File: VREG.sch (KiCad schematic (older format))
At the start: 100 parts

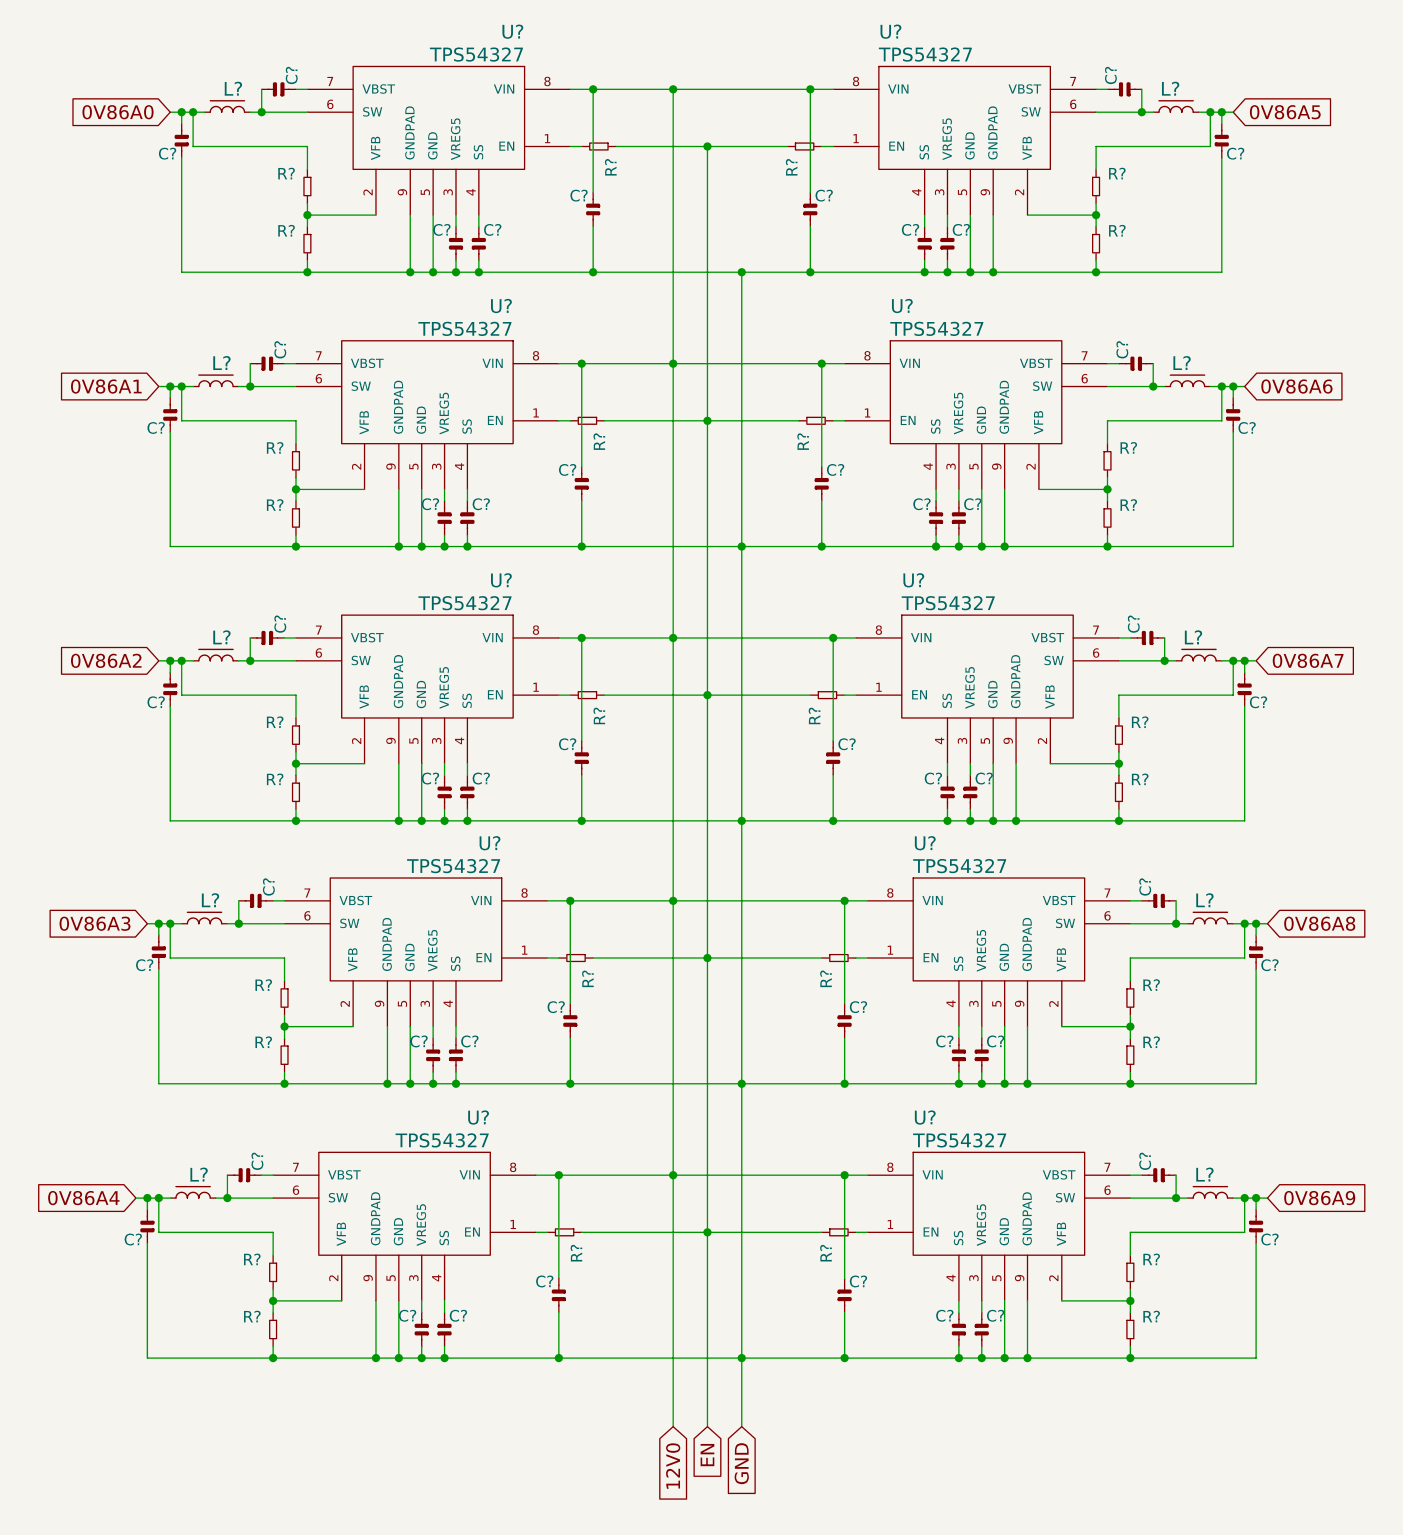
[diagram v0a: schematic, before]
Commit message: Fill in component values in schematic
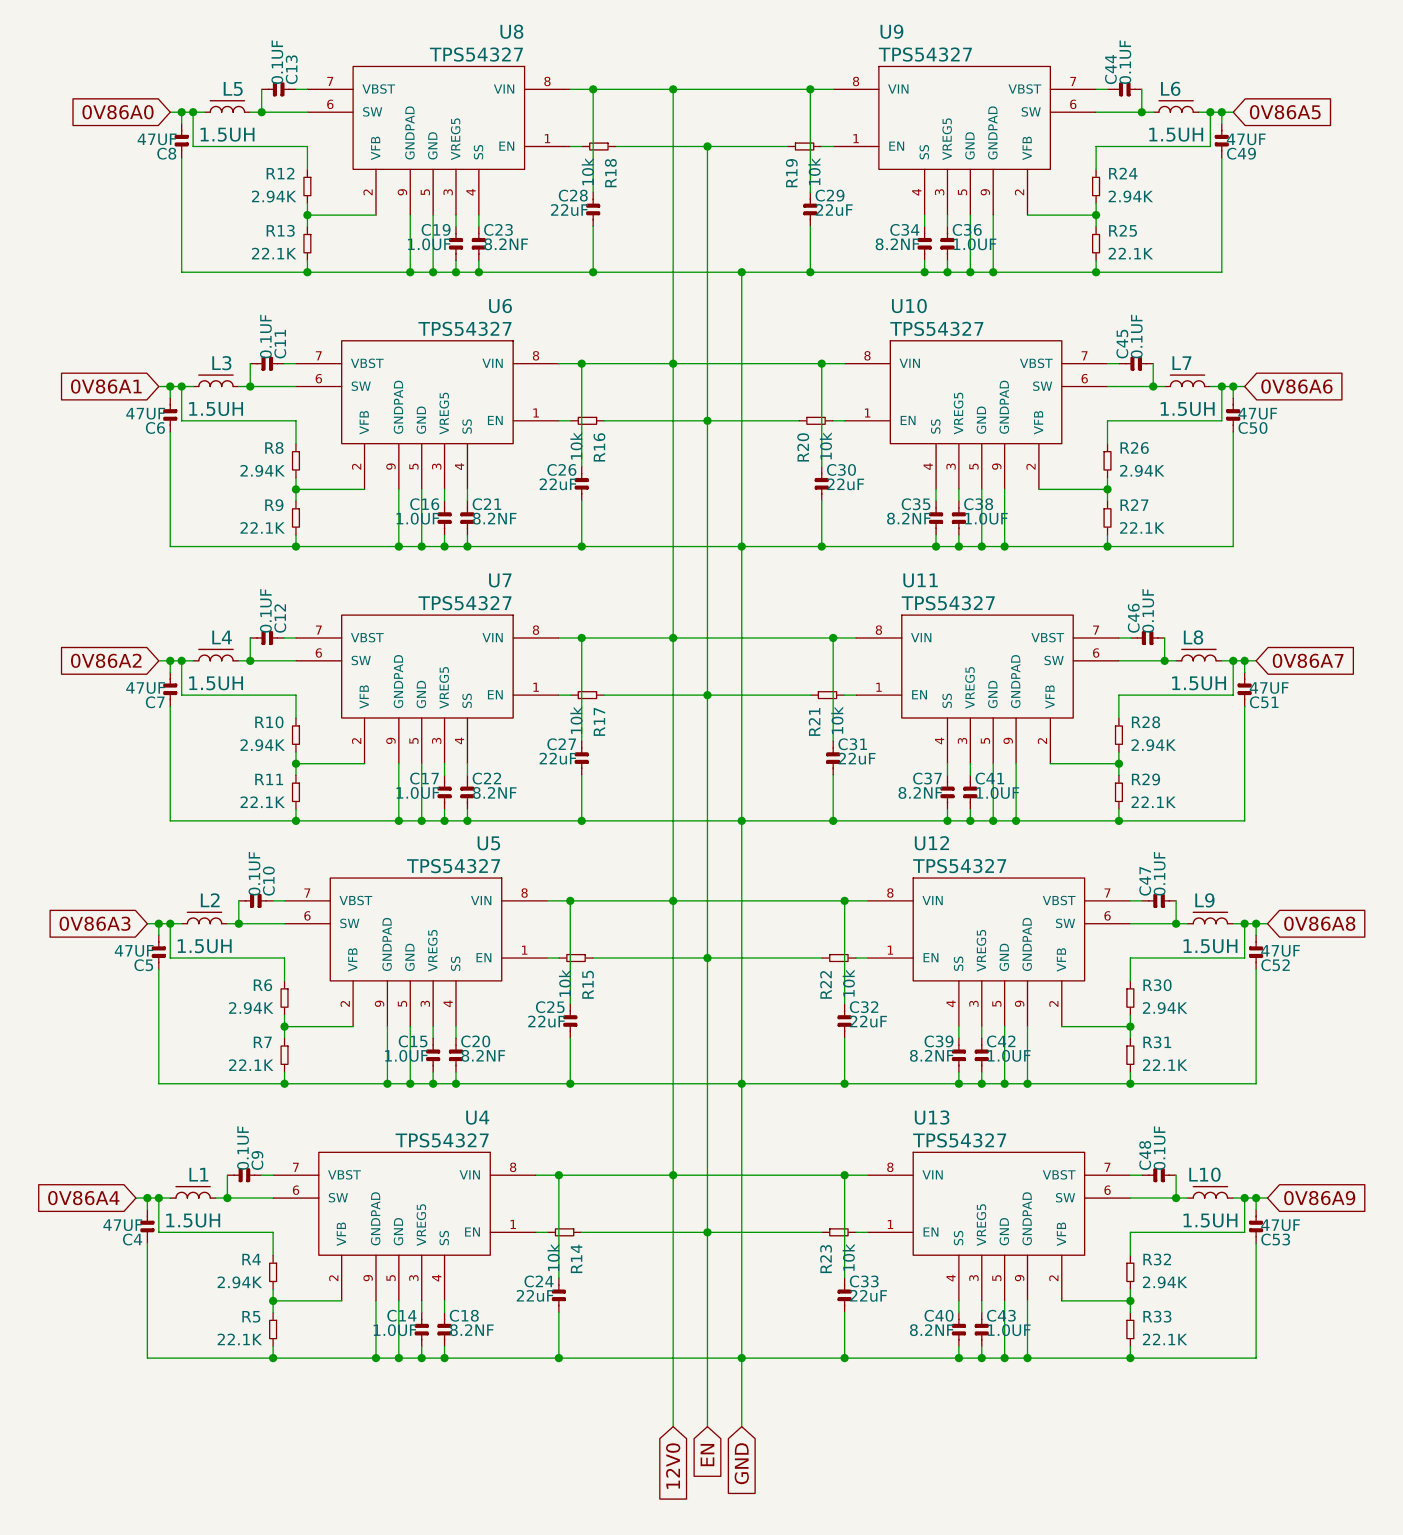
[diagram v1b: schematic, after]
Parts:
- C10, C11, C12, C13, C44, C45, C46, C47, C48, C9: renamed from C?; value CAPACITOR-NONPOLAR -> 0.1UF
- C14, C15, C16, C17, C19, C36, C38, C41, C42, C43: renamed from C?; value CAPACITOR-NONPOLAR -> 1.0UF
- C18, C20, C21, C22, C23, C34, C35, C37, C39, C40: renamed from C?; value CAPACITOR-NONPOLAR -> 8.2NF
- C24, C25, C26, C27, C28, C29, C30, C31, C32, C33: renamed from C?; value CAPACITOR-NONPOLAR -> 22uF
- C4, C49, C5, C50, C51, C52, C53, C6, C7, C8: renamed from C?; value CAPACITOR-NONPOLAR -> 47UF
- L1, L10, L2, L3, L4, L5, L6, L7, L8, L9: renamed from L?; value INDUCTOR-IRONCORE -> 1.5UH
- R10, R12, R24, R26, R28, R30, R32, R4, R6, R8: renamed from R?; value RESISTOR -> 2.94K
- R11, R13, R25, R27, R29, R31, R33, R5, R7, R9: renamed from R?; value RESISTOR -> 22.1K
- R14, R15, R16, R17, R18, R19, R20, R21, R22, R23: renamed from R?; value RESISTOR -> 10k
- gave numbers to parts that had none: 10

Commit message: Added ASIC row 0 and added links for power domains and comm lines
Renumbered components.

Added LED on MCP2210 GP3 pin to show SPI traffic activity (this feature
will require either programming of the NFx to modify NVRAM boot
settings [most likely], or added driver code in mcp init block [less
likely])
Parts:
- renumbered R9 to R10, R10 to R11, R11 to R12, R12 to R13, R13 to R14, R14 to R15, R15 to R16, R16 to R17, R17 to R18, R18 to R19, R19 to R20, R20 to R21, R21 to R22, R22 to R23, R23 to R24, R24 to R25, R25 to R26, R26 to R27, R27 to R28, R28 to R29, R29 to R30, R30 to R31, R31 to R32, R32 to R33, R33 to R34, R4 to R5, R5 to R6, R6 to R7, R7 to R8, R8 to R9
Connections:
- net EN renamed V_EN
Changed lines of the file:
@@
-EESchema Schematic File Version 2  date Sunday, February 23, 2014 'AMt' 01:58:09 AM
+EESchema Schematic File Version 2  date Monday, February 24, 2014 'AMt' 12:37:09 AM
 LIBS:power
 LIBS:74xgxx
@@
 Sheet 2 3
 Title "NanoFury NFx"
-Date "23 feb 2014"
+Date "24 feb 2014"
 Rev "43f0eac2"
 Comp ""
@@
 $EndComp
 $Comp
-L RESISTOR R18
+L RESISTOR R19
 U 1 1 53071CD3
 P 5250 1050
-F 0 "R18" H 5300 1000 50  0000 L BNN
+F 0 "R19" H 5300 1000 50  0000 L BNN
 F 1 "10k" H 5300 900 50  0000 L BNN
 F 2 "" H 5350 1150 50  0001 C CNN
@@
 $EndComp
 $Comp
-L RESISTOR R13
+L RESISTOR R14
 U 1 1 53071E4C
 P 3900 1400
-F 0 "R13" H 3950 1350 50  0000 L BNN
+F 0 "R14" H 3950 1350 50  0000 L BNN
 F 1 "22.1K" H 3950 1250 50  0000 L BNN
 F 2 "" H 4000 1500 50  0001 C CNN
@@
 $EndComp
 $Comp
-L RESISTOR R12
+L RESISTOR R13
 U 1 1 53071E5B
 P 3900 1150
-F 0 "R12" H 3950 1100 50  0000 L BNN
+F 0 "R13" H 3950 1100 50  0000 L BNN
 F 1 "2.94K" H 3950 1000 50  0000 L BNN
 F 2 "" H 4000 1250 50  0001 C CNN
@@
 $EndComp
 $Comp
-L RESISTOR R16
+L RESISTOR R17
 U 1 1 53071F77
 P 5200 2250
-F 0 "R16" H 5250 2200 50  0000 L BNN
+F 0 "R17" H 5250 2200 50  0000 L BNN
 F 1 "10k" H 5250 2100 50  0000 L BNN
 F 2 "" H 5300 2350 50  0001 C CNN
@@
 $EndComp
 $Comp
-L RESISTOR R9
+L RESISTOR R10
 U 1 1 53071F83
 P 3850 2600
-F 0 "R9" H 3900 2550 50  0000 L BNN
+F 0 "R10" H 3900 2550 50  0000 L BNN
 F 1 "22.1K" H 3900 2450 50  0000 L BNN
 F 2 "" H 3950 2700 50  0001 C CNN
@@
 $EndComp
 $Comp
-L RESISTOR R8
+L RESISTOR R9
 U 1 1 53071F89
 P 3850 2350
-F 0 "R8" H 3900 2300 50  0000 L BNN
+F 0 "R9" H 3900 2300 50  0000 L BNN
 F 1 "2.94K" H 3900 2200 50  0000 L BNN
 F 2 "" H 3950 2450 50  0001 C CNN
@@
 $EndComp
 $Comp
-L RESISTOR R17
+L RESISTOR R18
 U 1 1 53071FDA
 P 5200 3450
-F 0 "R17" H 5250 3400 50  0000 L BNN
+F 0 "R18" H 5250 3400 50  0000 L BNN
 F 1 "10k" H 5250 3300 50  0000 L BNN
 F 2 "" H 5300 3550 50  0001 C CNN
@@
 $EndComp
 $Comp
-L RESISTOR R11
+L RESISTOR R12
 U 1 1 53071FE6
 P 3850 3800
-F 0 "R11" H 3900 3750 50  0000 L BNN
+F 0 "R12" H 3900 3750 50  0000 L BNN
 F 1 "22.1K" H 3900 3650 50  0000 L BNN
 F 2 "" H 3950 3900 50  0001 C CNN
@@
 $EndComp
 $Comp
-L RESISTOR R10
+L RESISTOR R11
 U 1 1 53071FEC
 P 3850 3550
-F 0 "R10" H 3900 3500 50  0000 L BNN
+F 0 "R11" H 3900 3500 50  0000 L BNN
 F 1 "2.94K" H 3900 3400 50  0000 L BNN
 F 2 "" H 3950 3650 50  0001 C CNN
@@
 $EndComp
 $Comp
-L RESISTOR R15
+L RESISTOR R16
 U 1 1 5307203D
 P 5150 4600
-F 0 "R15" H 5200 4550 50  0000 L BNN
+F 0 "R16" H 5200 4550 50  0000 L BNN
 F 1 "10k" H 5200 4450 50  0000 L BNN
 F 2 "" H 5250 4700 50  0001 C CNN
@@
 $EndComp
 $Comp
-L RESISTOR R7
+L RESISTOR R8
 U 1 1 53072049
 P 3800 4950
-F 0 "R7" H 3850 4900 50  0000 L BNN
+F 0 "R8" H 3850 4900 50  0000 L BNN
 F 1 "22.1K" H 3850 4800 50  0000 L BNN
 F 2 "" H 3900 5050 50  0001 C CNN
@@
 $EndComp
 $Comp
-L RESISTOR R6
+L RESISTOR R7
 U 1 1 5307204F
 P 3800 4700
-F 0 "R6" H 3850 4650 50  0000 L BNN
+F 0 "R7" H 3850 4650 50  0000 L BNN
 F 1 "2.94K" H 3850 4550 50  0000 L BNN
 F 2 "" H 3900 4800 50  0001 C CNN
@@
 $EndComp
 $Comp
-L RESISTOR R19
+L RESISTOR R20
 U 1 1 530720A0
 P 6000 1050
-F 0 "R19" H 6050 1000 50  0000 L BNN
+F 0 "R20" H 6050 1000 50  0000 L BNN
 F 1 "10k" H 6050 900 50  0000 L BNN
 F 2 "" H 6100 1150 50  0001 C CNN
@@
 $EndComp
 $Comp
-L RESISTOR R25
+L RESISTOR R26
 U 1 1 530720AC
 P 7350 1400
-F 0 "R25" H 7400 1350 50  0000 L BNN
+F 0 "R26" H 7400 1350 50  0000 L BNN
 F 1 "22.1K" H 7400 1250 50  0000 L BNN
 F 2 "" H 7450 1500 50  0001 C CNN
@@
 $EndComp
 $Comp
-L RESISTOR R24
+L RESISTOR R25
 U 1 1 530720B2
 P 7350 1150
-F 0 "R24" H 7400 1100 50  0000 L BNN
+F 0 "R25" H 7400 1100 50  0000 L BNN
 F 1 "2.94K" H 7400 1000 50  0000 L BNN
 F 2 "" H 7450 1250 50  0001 C CNN
@@
 $EndComp
 $Comp
-L RESISTOR R20
+L RESISTOR R21
 U 1 1 53072103
 P 6050 2250
-F 0 "R20" H 6100 2200 50  0000 L BNN
+F 0 "R21" H 6100 2200 50  0000 L BNN
 F 1 "10k" H 6100 2100 50  0000 L BNN
 F 2 "" H 6150 2350 50  0001 C CNN
@@
 $EndComp
 $Comp
-L RESISTOR R27
+L RESISTOR R28
 U 1 1 5307210F
 P 7400 2600
-F 0 "R27" H 7450 2550 50  0000 L BNN
+F 0 "R28" H 7450 2550 50  0000 L BNN
 F 1 "22.1K" H 7450 2450 50  0000 L BNN
 F 2 "" H 7500 2700 50  0001 C CNN
@@
 $EndComp
 $Comp
-L RESISTOR R26
+L RESISTOR R27
 U 1 1 53072115
 P 7400 2350
-F 0 "R26" H 7450 2300 50  0000 L BNN
+F 0 "R27" H 7450 2300 50  0000 L BNN
 F 1 "2.94K" H 7450 2200 50  0000 L BNN
 F 2 "" H 7500 2450 50  0001 C CNN
@@
 $EndComp
 $Comp
-L RESISTOR R21
+L RESISTOR R22
 U 1 1 53072166
 P 6100 3450
-F 0 "R21" H 6150 3400 50  0000 L BNN
+F 0 "R22" H 6150 3400 50  0000 L BNN
 F 1 "10k" H 6150 3300 50  0000 L BNN
 F 2 "" H 6200 3550 50  0001 C CNN
@@
 $EndComp
 $Comp
-L RESISTOR R29
+L RESISTOR R30
 U 1 1 53072172
 P 7450 3800
-F 0 "R29" H 7500 3750 50  0000 L BNN
+F 0 "R30" H 7500 3750 50  0000 L BNN
 F 1 "22.1K" H 7500 3650 50  0000 L BNN
 F 2 "" H 7550 3900 50  0001 C CNN
@@
 $EndComp
 $Comp
-L RESISTOR R28
+L RESISTOR R29
 U 1 1 53072178
 P 7450 3550
-F 0 "R28" H 7500 3500 50  0000 L BNN
+F 0 "R29" H 7500 3500 50  0000 L BNN
 F 1 "2.94K" H 7500 3400 50  0000 L BNN
 F 2 "" H 7550 3650 50  0001 C CNN
@@
 $EndComp
 $Comp
-L RESISTOR R22
+L RESISTOR R23
 U 1 1 530721C9
 P 6150 4600
-F 0 "R22" H 6200 4550 50  0000 L BNN
+F 0 "R23" H 6200 4550 50  0000 L BNN
 F 1 "10k" H 6200 4450 50  0000 L BNN
 F 2 "" H 6250 4700 50  0001 C CNN
@@
 $EndComp
 $Comp
-L RESISTOR R31
+L RESISTOR R32
 U 1 1 530721D5
 P 7500 4950
-F 0 "R31" H 7550 4900 50  0000 L BNN
+F 0 "R32" H 7550 4900 50  0000 L BNN
 F 1 "22.1K" H 7550 4800 50  0000 L BNN
 F 2 "" H 7600 5050 50  0001 C CNN
@@
 $EndComp
 $Comp
-L RESISTOR R30
+L RESISTOR R31
 U 1 1 530721DB
 P 7500 4700
-F 0 "R30" H 7550 4650 50  0000 L BNN
+F 0 "R31" H 7550 4650 50  0000 L BNN
 F 1 "2.94K" H 7550 4550 50  0000 L BNN
 F 2 "" H 7600 4800 50  0001 C CNN
@@
 $EndComp
 $Comp
-L RESISTOR R14
+L RESISTOR R15
 U 1 1 5307222C
 P 5100 5800
-F 0 "R14" H 5150 5750 50  0000 L BNN
+F 0 "R15" H 5150 5750 50  0000 L BNN
 F 1 "10k" H 5150 5650 50  0000 L BNN
 F 2 "" H 5200 5900 50  0001 C CNN
@@
 $EndComp
 $Comp
-L RESISTOR R5
+L RESISTOR R6
 U 1 1 53072238
 P 3750 6150
-F 0 "R5" H 3800 6100 50  0000 L BNN
+F 0 "R6" H 3800 6100 50  0000 L BNN
 F 1 "22.1K" H 3800 6000 50  0000 L BNN
 F 2 "" H 3850 6250 50  0001 C CNN
@@
 $EndComp
 $Comp
-L RESISTOR R4
+L RESISTOR R5
 U 1 1 5307223E
 P 3750 5900
-F 0 "R4" H 3800 5850 50  0000 L BNN
+F 0 "R5" H 3800 5850 50  0000 L BNN
 F 1 "2.94K" H 3800 5750 50  0000 L BNN
 F 2 "" H 3850 6000 50  0001 C CNN
@@
 $EndComp
 $Comp
-L RESISTOR R23
+L RESISTOR R24
 U 1 1 5307228F
 P 6150 5800
-F 0 "R23" H 6200 5750 50  0000 L BNN
+F 0 "R24" H 6200 5750 50  0000 L BNN
 F 1 "10k" H 6200 5650 50  0000 L BNN
 F 2 "" H 6250 5900 50  0001 C CNN
@@
 $EndComp
 $Comp
-L RESISTOR R33
+L RESISTOR R34
 U 1 1 5307229B
 P 7500 6150
-F 0 "R33" H 7550 6100 50  0000 L BNN
+F 0 "R34" H 7550 6100 50  0000 L BNN
 F 1 "22.1K" H 7550 6000 50  0000 L BNN
 F 2 "" H 7600 6250 50  0001 C CNN
@@
 $EndComp
 $Comp
-L RESISTOR R32
+L RESISTOR R33
 U 1 1 530722A1
 P 7500 5900
-F 0 "R32" H 7550 5850 50  0000 L BNN
+F 0 "R33" H 7550 5850 50  0000 L BNN
 F 1 "2.94K" H 7550 5750 50  0000 L BNN
 F 2 "" H 7600 6000 50  0001 C CNN
@@
 $EndComp
 Text GLabel 5650 6650 3    60   Input ~ 0
-EN
+V_EN
 Text GLabel 5800 6650 3    60   Input ~ 0
 GND
